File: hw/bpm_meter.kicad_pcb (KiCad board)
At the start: 2 copper layers, 60 x 44 mm, 85 parts, among them J1 Conn_01x06_Pin, J2 Conn_01x03_Pin, J901 USB_C_Receptacle_USB2.0, Q1 AO3400A, SW901 SW_MEC_5E, U1 AOZ1282CI, U10 IS31FL3236A, U11 SLS0391FR1A1GD, U12 SLS0391FR1A1GD, U13 SLS0391FR1A1GD, U2 AMS1117-3.3, U3 H11L1, U901 RP2040, U902 AMS1117-3.3, U903 W25Q128JVS, Y901 Crystal_GND24_Small

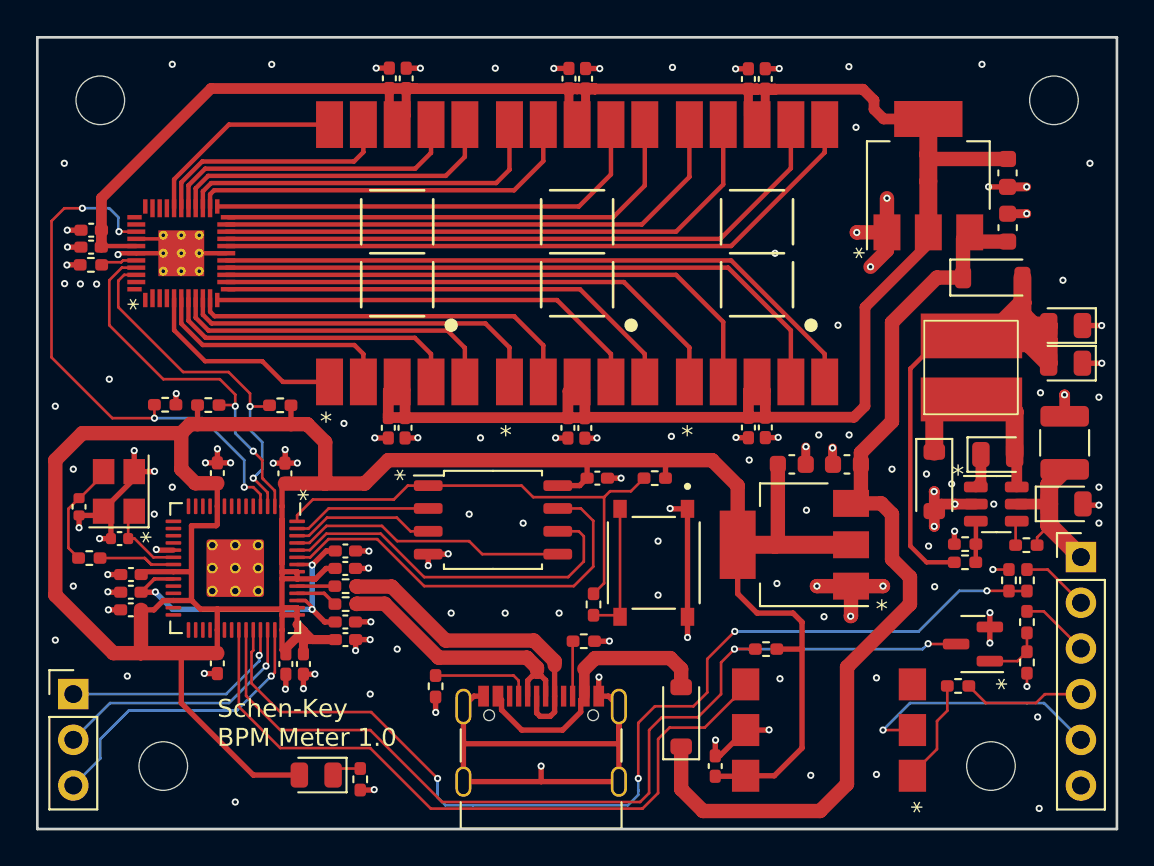
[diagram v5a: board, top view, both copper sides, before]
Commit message: Hardware v1.0 taped-out to JLCPCB on 06.01.2024
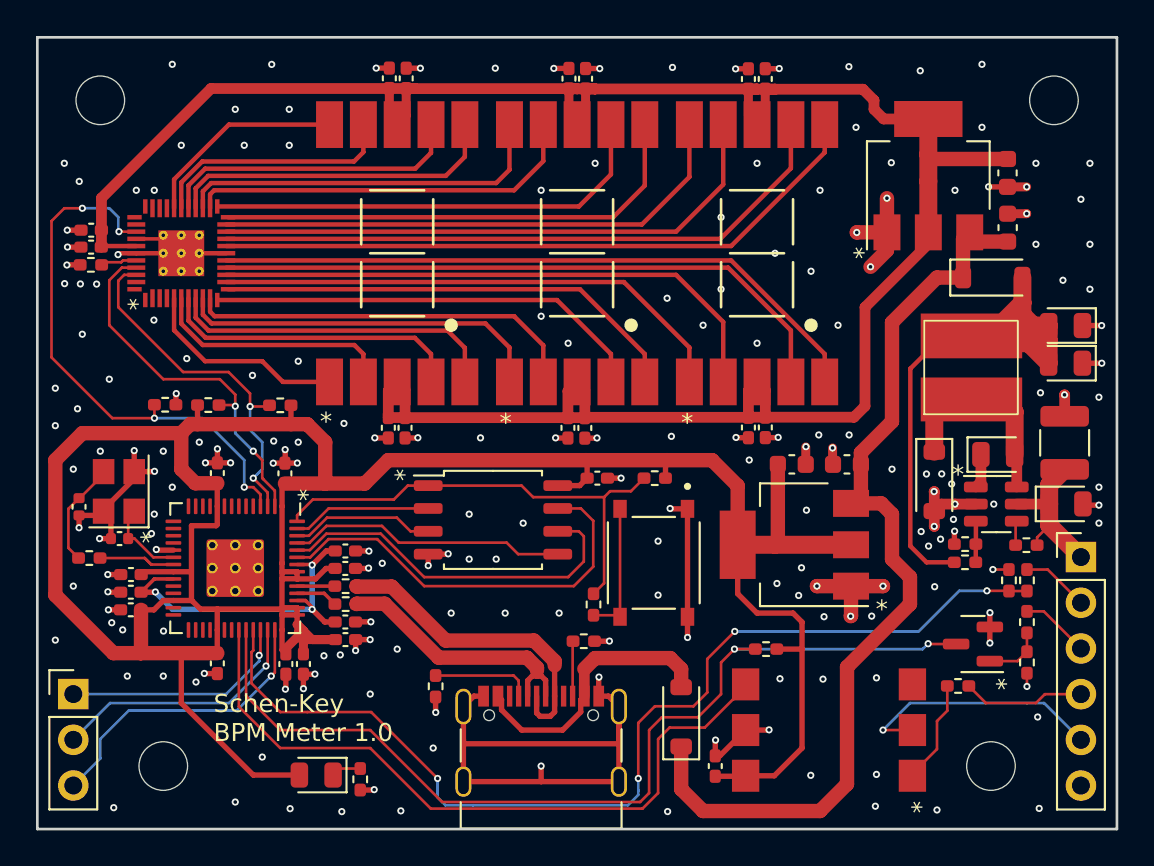
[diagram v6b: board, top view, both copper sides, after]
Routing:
- net +3V3: track 171.6 -> 169.0 mm
- net GND: vias 133 -> 202
